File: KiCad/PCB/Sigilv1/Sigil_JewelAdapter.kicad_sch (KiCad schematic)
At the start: 3 parts, among them J1 ADAFRUIT NEOPIXEL JEWEL 7 RGBW, J2 PIGTAIL TO SIGIL J5

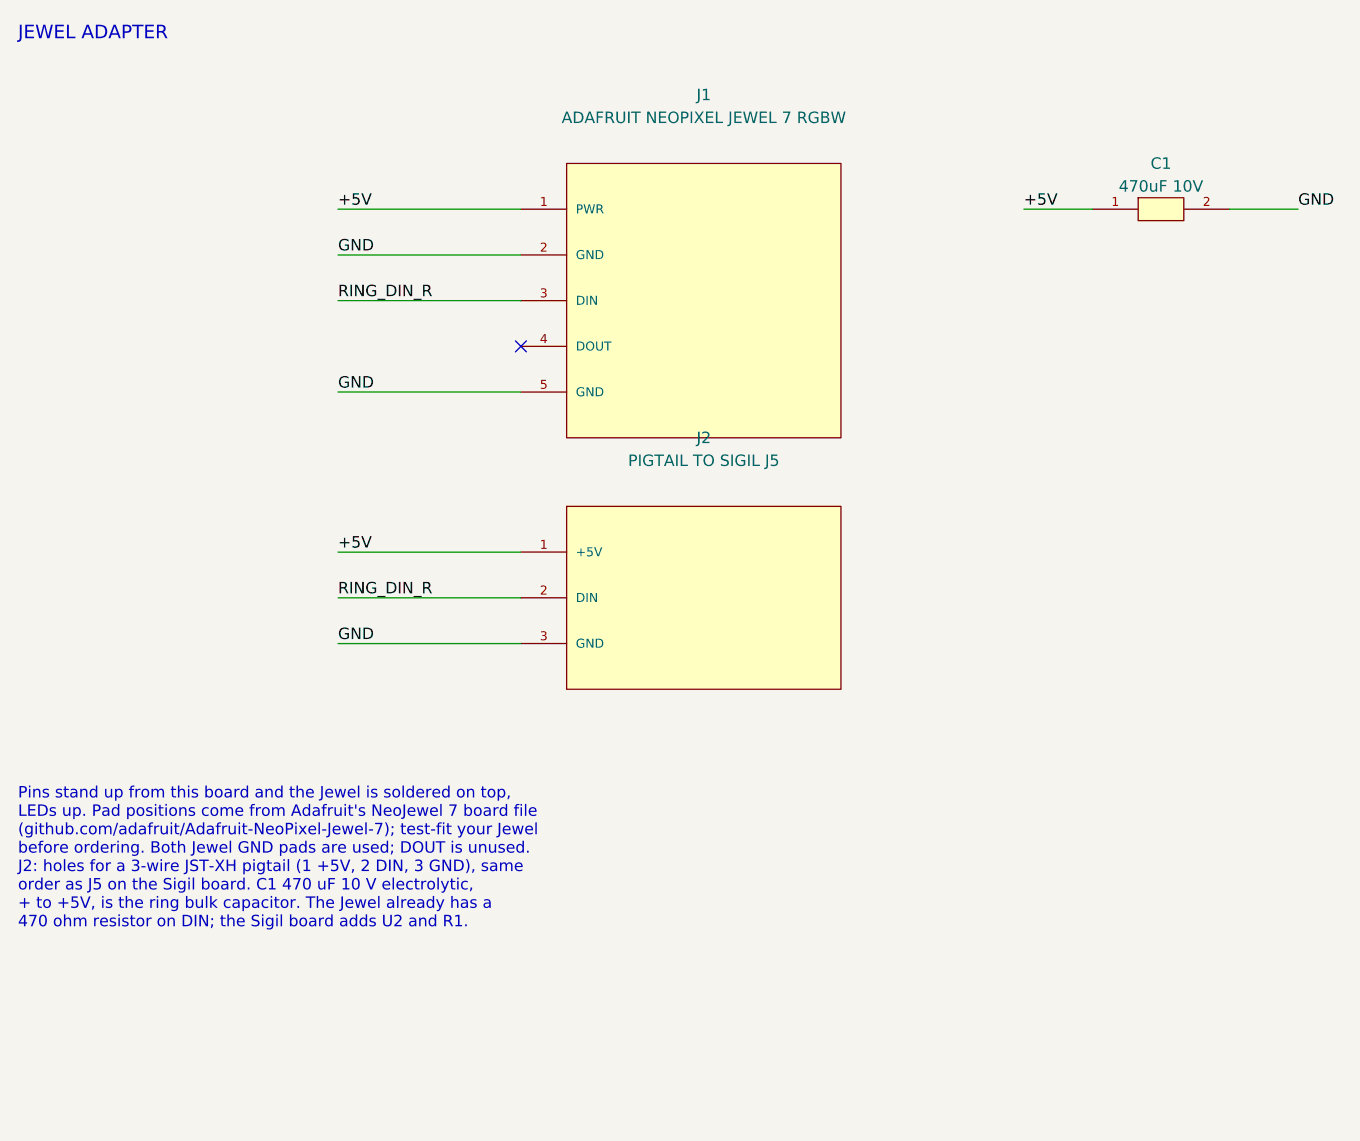
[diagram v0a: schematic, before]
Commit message: Jewel adapter: optional chain-out for more pixels after the ring
Co-Authored-By: Claude Opus 5.5 <noreply@anthropic.com>
Claude-Session: https://claude.ai/code/session_01EuTMd98XaCZ1DRqGGQFyaV
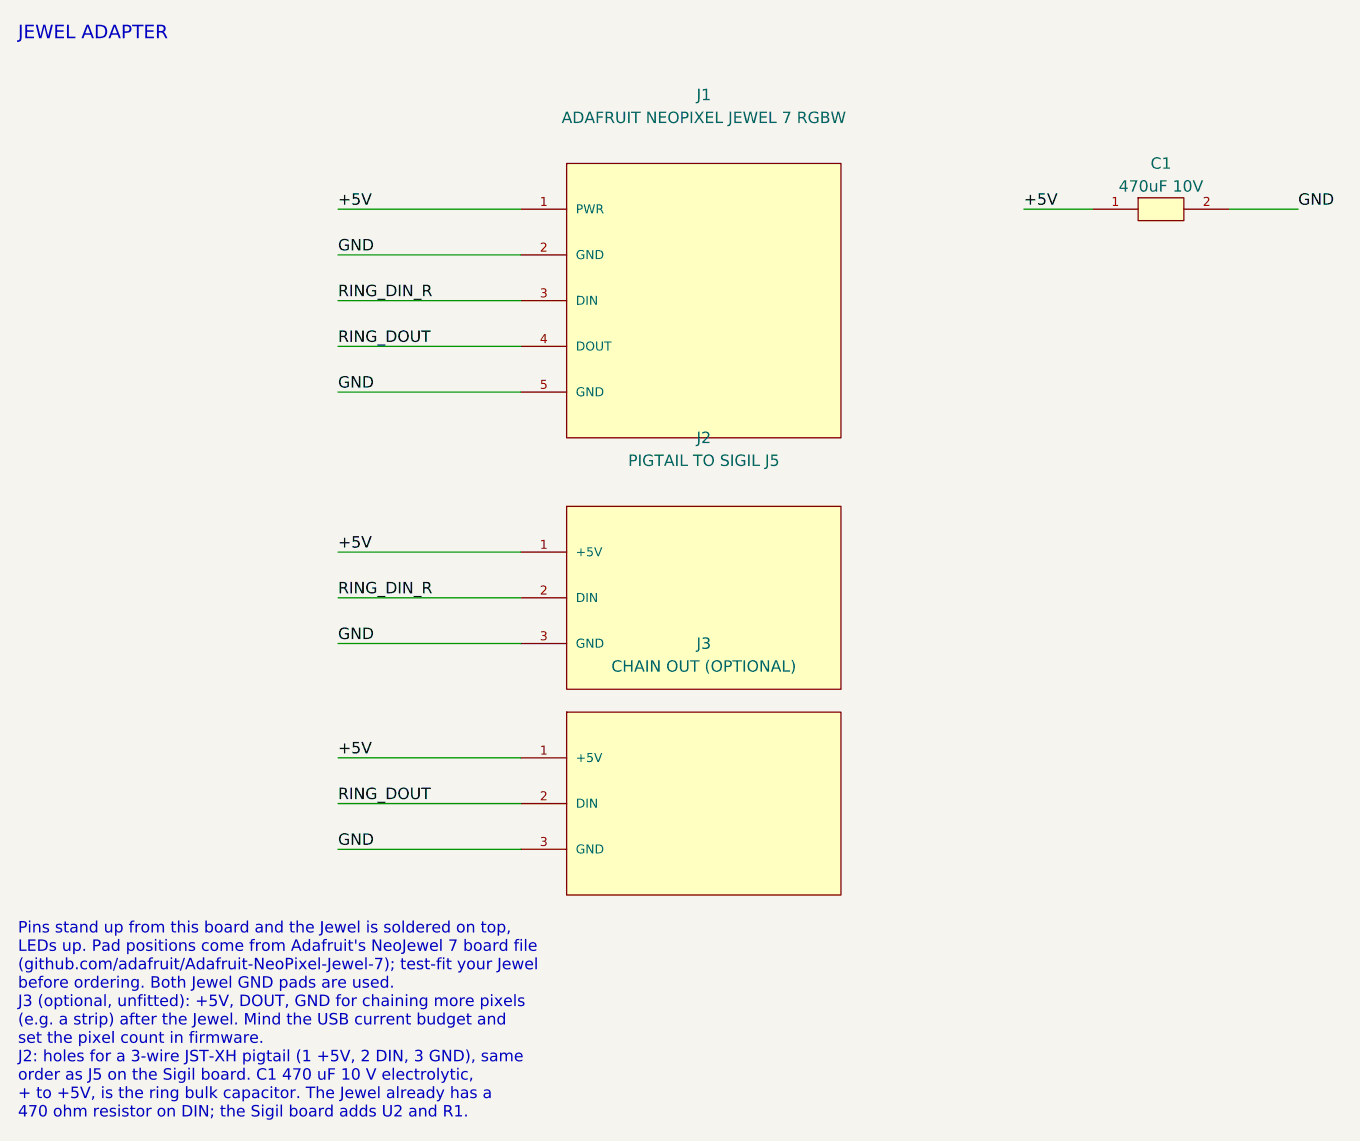
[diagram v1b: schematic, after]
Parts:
- added J3: CHAIN OUT (OPTIONAL), Connector_PinHeader_2.54mm:PinHeader_1x03_P2.54mm_Vertical, symbol Sigil:Pigtail_Pads_3
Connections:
- net +5V: now also J3.1 (+5V)
- net GND: now also J3.3 (GND)
- net RING_DOUT: now reaches J1.4 (DOUT)
- net RING_DOUT: now also J3.2 (DIN)
- no-connect marks 1 -> 0
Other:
- note added: "Pins stand up from this board and the Jewel is soldered on top, LEDs up. Pad positions come from Adafruit's NeoJewel 7 board file (github.com/adafruit/Adafruit-NeoPixel-Jewel-7); test-fit your Jewel before ordering. Both Jewel GND pads are used. J3 (optional, unfitted): +5V, DOUT, GND for chaining more pixels (e.g. a strip) after the Jewel. Mind the USB current budget and set the pixel count in f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"
- note removed: "Pins stand up from this board and the Jewel is soldered on top, LEDs up. Pad positions come from Adafruit's NeoJewel 7 board file (github.com/adafruit/Adafruit-NeoPixel-Jewel-7); test-fit your Jewel before ordering. Both Jewel GND pads are used; DOUT is unused. J2: holes for a 3-wire JST-XH pigtail (1 +5V, 2 DIN, 3 GND), same order as J5 on the Sigil board. C1 470 uF 10 V electrolytic, + to +5V, 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"
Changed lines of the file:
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@@
 (wire (pts (xy 81.28 55.88) (xy 60.96 55.88)) (stroke (width 0) (type default)))
 (label "RING_DIN_R" (at 60.96 55.88 0) (effects (font (size 1.27 1.27)) (justify left bottom)))
-(no_connect (at 81.28 60.96))
+(wire (pts (xy 81.28 60.96) (xy 60.96 60.96)) (stroke (width 0) (type default)))
+(label "RING_DOUT" (at 60.96 60.96 0) (effects (font (size 1.27 1.27)) (justify left bottom)))
 (wire (pts (xy 81.28 66.04) (xy 60.96 66.04)) (stroke (width 0) (type default)))
 (label "GND" (at 60.96 66.04 0) (effects (font (size 1.27 1.27)) (justify left bottom)))
@@
 (wire (pts (xy 81.28 93.98) (xy 60.96 93.98)) (stroke (width 0) (type default)))
 (label "GND" (at 60.96 93.98 0) (effects (font (size 1.27 1.27)) (justify left bottom)))
+(symbol (lib_id "Sigil:Pigtail_Pads_3") (at 101.6 106.68 0) (unit 1) (in_bom yes) (on_board yes) (dnp no)
+ (property "Reference" "J3" (at 101.6 93.98 0)  (effects (font (size 1.27 1.27))))(property "Value" "CHAIN OUT (OPTIONAL)" (at 101.6 96.52000000000001 0)  (effects (font (size 1.27 1.27)))) (property "Footprint" "Connector_PinHeader_2.54mm:PinHeader_1x03_P2.54mm_Vertical" (at 101.6 106.68 0) (hide yes) (effects (font (size 1.27 1.27)))) (pin "1")(pin "2")(pin "3")
+      (instances (project "Sigil_JewelAdapter" (path "/6b1d3f52-0c4e-4a8e-9f7a-2d5c8e1b9a03" (reference "J3") (unit 1)))))
+(wire (pts (xy 81.28 106.68) (xy 60.96 106.68)) (stroke (width 0) (type default)))
+(label "+5V" (at 60.96 106.68 0) (effects (font (size 1.27 1.27)) (justify left bottom)))
+(wire (pts (xy 81.28 111.76) (xy 60.96 111.76)) (stroke (width 0) (type default)))
+(label "RING_DOUT" (at 60.96 111.76 0) (effects (font (size 1.27 1.27)) (justify left bottom)))
+(wire (pts (xy 81.28 116.84) (xy 60.96 116.84)) (stroke (width 0) (type default)))
+(label "GND" (at 60.96 116.84 0) (effects (font (size 1.27 1.27)) (justify left bottom)))
 (symbol (lib_id "Sigil:Capacitor") (at 152.4 45.72 0) (unit 1) (in_bom yes) (on_board yes) (dnp no)
  (property "Reference" "C1" (at 152.4 40.64 0)  (effects (font (size 1.27 1.27))))(property "Value" "470uF 10V" (at 152.4 43.18 0)  (effects (font (size 1.27 1.27)))) (property "Footprint" "Capacitor_THT:CP_Radial_D8.0mm_P3.50mm" (at 152.4 45.72 0) (hide yes) (effects (font (size 1.27 1.27)))) (pin "1")(pin "2")
@@
 (wire (pts (xy 160.02 45.72) (xy 167.64 45.72)) (stroke (width 0) (type default)))
 (label "GND" (at 167.64 45.72 0) (effects (font (size 1.27 1.27)) (justify left bottom)))
-(text "Pins stand up from this board and the Jewel is soldered on top,\nLEDs up. Pad positions come from Adafruit's NeoJewel 7 board file\n(github.com/adafruit/Adafruit-NeoPixel-Jewel-7); test-fit your Jewel\nbefore ordering. Both Jewel GND pads are used; DOUT is unused.\nJ2: holes for a 3-wire JST-XH pigtail (1 +5V, 2 DIN, 3 GND), same\norder as J5 on the Sigil board. C1 470 uF 10 V electrolytic,\n+ to +5V, is the ring bulk capacitor. The Jewel already has a\n470 ohm resistor on DIN; the Sigil board adds U2 and R1." (at 25.4 110 0) (effects (font (size 1.27 1.27)) (justify left top)))
+(text "Pins stand up from this board and the Jewel is soldered on top,\nLEDs up. Pad positions come from Adafruit's NeoJewel 7 board file\n(github.com/adafruit/Adafruit-NeoPixel-Jewel-7); test-fit your Jewel\nbefore ordering. Both Jewel GND pads are used.\nJ3 (optional, unfitted): +5V, DOUT, GND for chaining more pixels\n(e.g. a strip) after the Jewel. Mind the USB current budget and\nset the pixel count in firmware.\nJ2: holes for a 3-wire JST-XH pigtail (1 +5V, 2 DIN, 3 GND), same\norder as J5 on the Sigil board. C1 470 uF 10 V electrolytic,\n+ to +5V, is the ring bulk capacitor. The Jewel already has a\n470 ohm resistor on DIN; the Sigil board adds U2 and R1." (at 25.4 125 0) (effects (font (size 1.27 1.27)) (justify left top)))
 (embedded_fonts no))

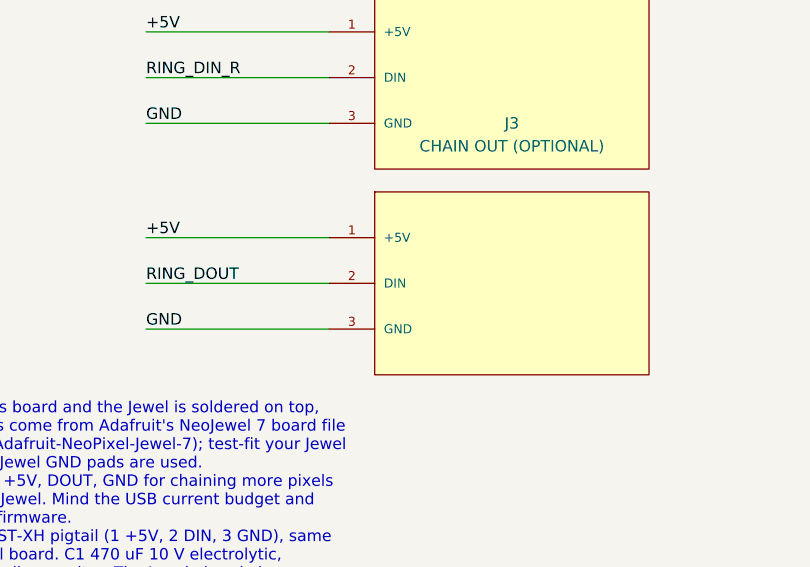
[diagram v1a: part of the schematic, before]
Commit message: Sigil schematic review fixes
- DevKit footprint courtyard was skewed (two slanted edges); draw Fab,
  silk and courtyard as true rectangles.
- Chain-out J3 gets its own symbol (pin 2 named DOUT, not DIN).
- Stale comments and docs: U2 is SMD, U1 has a footprint, strip chaining
  is from the adapter's J3; verifier PASS line names what it checked.

Co-Authored-By: Claude Opus 5.5 <noreply@anthropic.com>
Claude-Session: https://claude.ai/code/session_01EuTMd98XaCZ1DRqGGQFyaV
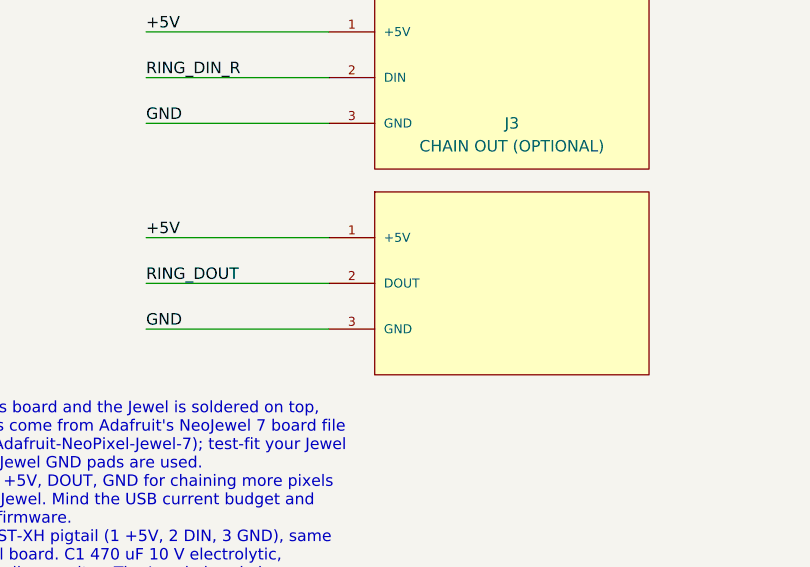
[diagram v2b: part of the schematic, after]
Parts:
- J3: symbol Sigil:Pigtail_Pads_3 -> Sigil:Chain_Out_Pads_3
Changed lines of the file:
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@@
 (wire (pts (xy 81.28 93.98) (xy 60.96 93.98)) (stroke (width 0) (type default)))
 (label "GND" (at 60.96 93.98 0) (effects (font (size 1.27 1.27)) (justify left bottom)))
-(symbol (lib_id "Sigil:Pigtail_Pads_3") (at 101.6 106.68 0) (unit 1) (in_bom yes) (on_board yes) (dnp no)
+(symbol (lib_id "Sigil:Chain_Out_Pads_3") (at 101.6 106.68 0) (unit 1) (in_bom yes) (on_board yes) (dnp no)
  (property "Reference" "J3" (at 101.6 93.98 0)  (effects (font (size 1.27 1.27))))(property "Value" "CHAIN OUT (OPTIONAL)" (at 101.6 96.52000000000001 0)  (effects (font (size 1.27 1.27)))) (property "Footprint" "Connector_PinHeader_2.54mm:PinHeader_1x03_P2.54mm_Vertical" (at 101.6 106.68 0) (hide yes) (effects (font (size 1.27 1.27)))) (pin "1")(pin "2")(pin "3")
       (instances (project "Sigil_JewelAdapter" (path "/6b1d3f52-0c4e-4a8e-9f7a-2d5c8e1b9a03" (reference "J3") (unit 1)))))
